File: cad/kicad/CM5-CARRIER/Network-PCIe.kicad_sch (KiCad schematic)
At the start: 59 parts, among them J610 74991114412, J611 74991114412, J612 74991114412, J613 74991114412, J620 AW7915-NP1_WIFI6_4T4R, J621 PCIE_SPARE_TEST, U601 PI7C9X2G608GP, U611 LAN7430, U612 LAN7430, U613 LAN7430, U630 TPD4E05U06DQA, U631 TPD4E05U06DQA, U632 TPD4E05U06DQA, U633 TPD4E05U06DQA, U634 TPD4E05U06DQA, U635 TPD4E05U06DQA, U636 TPD4E05U06DQA, U637 TPD4E05U06DQA, Y611 25MHz, Y612 25MHz, Y613 25MHz

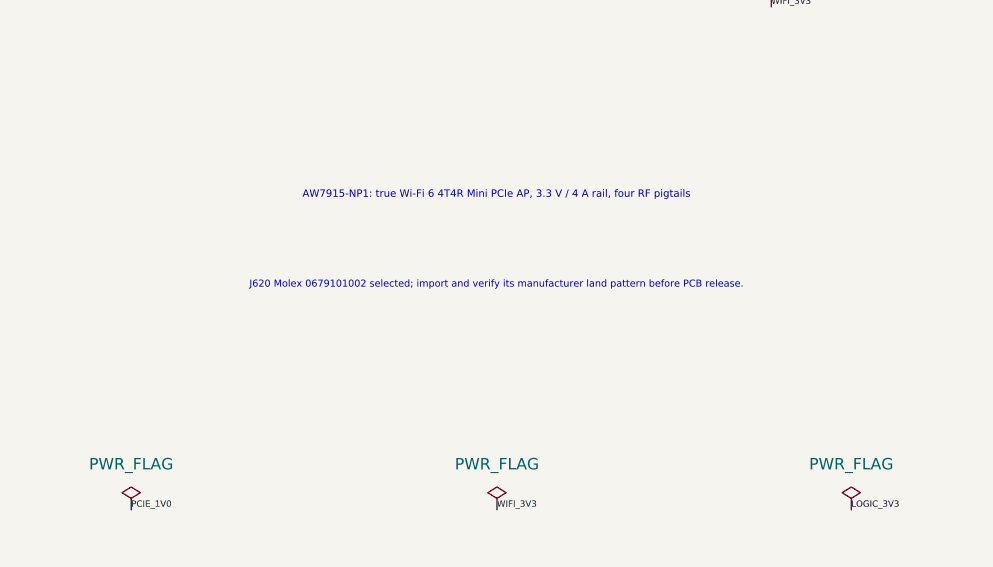
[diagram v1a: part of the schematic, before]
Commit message: Add controlled connector footprint audit
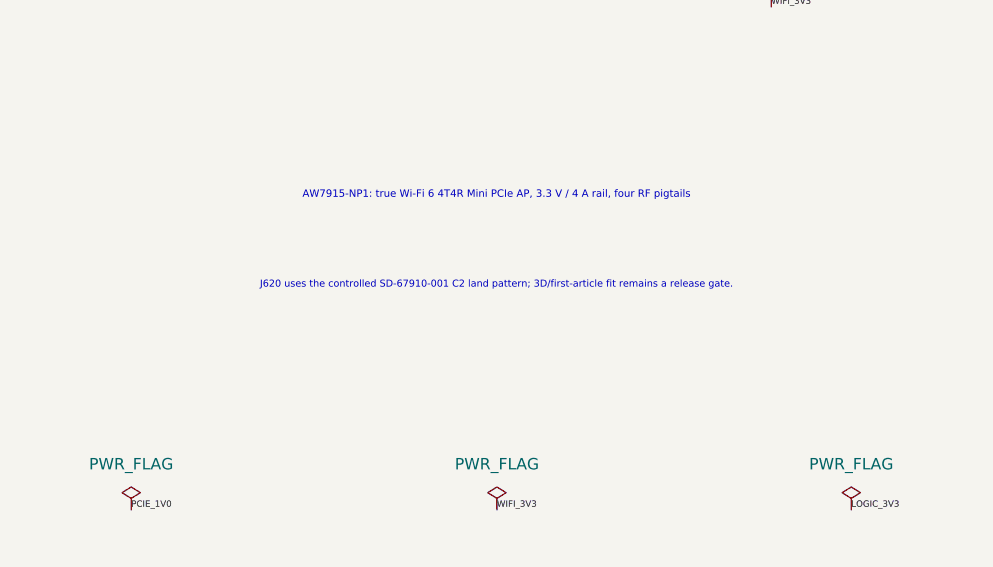
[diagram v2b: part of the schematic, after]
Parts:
- J620: footprint (none) -> CM5Carrier:Molex_0679101002_Mini_PCIe
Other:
- note added: "J620 uses the controlled SD-67910-001 C2 land pattern; 3D/first-article fit remains a release gate."
- note removed: "J620 Molex 0679101002 selected; import and verify its manufacturer land pattern before PCB release."
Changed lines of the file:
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@@
 			)
 		)
+		(property "Footprint" "CM5Carrier:Molex_0679101002_Mini_PCIe"
+			(at 515.62 420.37 0.0000)
+			(effects
+				(font
+					(size 1.27 1.27)
+				)
+				(hide yes)
+			)
+		)
 		(property "Manufacturer" "Molex"
 			(at 518.16 425.4499 0)
@@
 		)
 	)
-	(text "J620 Molex 0679101002 selected; import and verify its manufacturer land pattern before PCB release."
+	(text "J620 uses the controlled SD-67910-001 C2 land pattern; 3D/first-article fit remains a release gate."
 		(exclude_from_sim no)
 		(at 400 525 0.0000)

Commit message: Complete A1 detailed carrier and audio capture
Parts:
- removed C6121: 10uF, symbol Device:C
- removed C6122: 100nF, symbol Device:C
- removed J621: PCIE_SPARE_TEST, symbol Connector_Generic:Conn_02x06_Odd_Even
- removed L6121: 3.3uH, symbol Device:L
- removed U636: TPD4E05U06DQA, Package_SON:USON-10_2.5x1.0mm_P0.5mm, symbol Power_Protection:TPD4E05U06DQA
- removed Y611, Y613: 25MHz, symbol Device:Crystal
- added C6114, C6115, C6124, C6125, C6134, C6135: 15pF C0G, Capacitor_SMD:C_0402_1005Metric, symbol Device:C
- added J612: 74991114412, CM5Carrier:T_Wurth_WE-RJ45LAN_74991114412, symbol WurthRJ45:74991114412
- added R6122: 6.04k 1%, Resistor_SMD:R_0603_1608Metric, symbol Device:R
- added R657: 330R, Resistor_SMD:R_0603_1608Metric, symbol Device:R
- added Y611, Y612, Y613: 25MHz / 10pF / -40..85C, Crystal:Crystal_SMD_3225-4Pin_3.2x2.5mm, symbol CM5Carrier:Crystal_GND24_3225
- C601, C602, C603, C604, C6112, C6132: footprint (none) -> Capacitor_SMD:C_0402_1005Metric; MPN (none) -> C1005X7R1H104K050BB; Manufacturer (none) -> TDK
- C6111, C6131: value 10uF -> 10uF 25V X5R; footprint (none) -> Capacitor_SMD:C_0603_1608Metric; MPN (none) -> GRM188R61E106MA73D; Manufacturer (none) -> Murata
- C6113, C6133: value 1uF ESR>=0.1R -> 1uF 35V X5R / ESR <1R; footprint (none) -> Capacitor_SMD:C_0402_1005Metric; MPN (none) -> GRM155R6YA105KE11D; Manufacturer (none) -> Murata
- C6121: renamed from R6121; value 200R 1% -> 10uF 25V X5R; footprint (none) -> Capacitor_SMD:C_0603_1608Metric; symbol Device:R -> Device:C; MPN (none) -> GRM188R61E106MA73D; Manufacturer (none) -> Murata
- C6122: renamed from R6122; value 6.04k 1% -> 100nF; footprint (none) -> Capacitor_SMD:C_0402_1005Metric; symbol Device:R -> Device:C; MPN (none) -> C1005X7R1H104K050BB; Manufacturer (none) -> TDK
- C6123: renamed from Y612; value 25MHz -> 1uF 35V X5R / ESR <1R; footprint (none) -> Capacitor_SMD:C_0402_1005Metric; symbol Device:Crystal -> Device:C; MPN (none) -> GRM155R6YA105KE11D; Manufacturer (none) -> Murata
- L6111, L6131: value 3.3uH -> 3.3uH / 2.37A min; footprint (none) -> CM5Carrier:TDK_VLS3012HBX; MPN (none) -> VLS3012HBX-3R3M-N; Manufacturer (none) -> TDK
- L6121: renamed from C6123; value 1uF ESR>=0.1R -> 3.3uH / 2.37A min; footprint (none) -> CM5Carrier:TDK_VLS3012HBX; symbol Device:C -> Device:L; MPN (none) -> VLS3012HBX-3R3M-N; Manufacturer (none) -> TDK
- R601: footprint (none) -> Resistor_SMD:R_0603_1608Metric; MPN (none) -> RC0603FR-074K7L; Manufacturer (none) -> Yageo
- R602, R603: footprint (none) -> Resistor_SMD:R_0603_1608Metric; MPN (none) -> RC0603FR-071K43L; Manufacturer (none) -> Yageo
- R604: footprint (none) -> Resistor_SMD:R_0603_1608Metric; MPN (none) -> RC0603FR-07475RL; Manufacturer (none) -> Yageo
- R605, R606: footprint (none) -> Resistor_SMD:R_0603_1608Metric; MPN (none) -> RC0603FR-072K2L; Manufacturer (none) -> Yageo
- R607: footprint (none) -> Resistor_SMD:R_0603_1608Metric; MPN (none) -> RC0603JR-070RL; Manufacturer (none) -> Yageo
- R6111, R6131: footprint (none) -> Resistor_SMD:R_0603_1608Metric; MPN (none) -> RC0603FR-07200RL; Manufacturer (none) -> Yageo
- R6112, R6132: footprint (none) -> Resistor_SMD:R_0603_1608Metric; MPN (none) -> RC0603FR-076K04L; Manufacturer (none) -> Yageo
- R6121: renamed from J612; value 74991114412 -> 200R 1%; footprint CM5Carrier:T_Wurth_WE-RJ45LAN_74991114412 -> Resistor_SMD:R_0603_1608Metric; symbol WurthRJ45:74991114412 -> Device:R; MPN 74991114412 -> RC0603FR-07200RL; Manufacturer Wurth Elektronik -> Yageo
- R620: footprint (none) -> Resistor_SMD:R_0603_1608Metric; MPN (none) -> RC0603FR-0710KL; Manufacturer (none) -> Yageo
- R650, R651, R652, R653, R654, R655, R656: footprint (none) -> Resistor_SMD:R_0603_1608Metric; MPN (none) -> RC0603FR-07330RL; Manufacturer (none) -> Yageo
- U601: MPN (none) -> PI7C9X2G608GPCNJEX; Manufacturer (none) -> Diodes Incorporated
- U611, U612, U613: MPN LAN7430/Y9X -> LAN7430T-I/Y9X
- U630, U631, U632, U633, U634, U635, U637: MPN TPD4E05U06DQA -> TPD4E05U06DQAR
- U636: renamed from R657; value 330R -> TPD4E05U06DQA; footprint (none) -> Package_SON:USON-10_2.5x1.0mm_P0.5mm; symbol Device:R -> Power_Protection:TPD4E05U06DQA; MPN (none) -> TPD4E05U06DQAR; Manufacturer (none) -> Texas Instruments
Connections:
- net CHASSIS_GND: now also J612.S1 (SHIELD1), J612.S2 (SHIELD2); no longer R6121.S1 (SHIELD1), R6121.S2 (SHIELD2)
- net GND: now also C6123.2, R6121.2, U636.3 (GND), U636.8 (GND), C6114.2, C6115.2, C6124.2, C6125.2, C6134.2, C6135.2, J612.1 (GND), R6122.2, Y611.2 (GND), Y611.4 (GND), Y612.2 (GND), Y612.4 (GND), Y613.2 (GND), Y613.4 (GND); no longer L6121.2, R6121.1 (GND)
- net LAN1_1V2: now also C6121.1, C6122.1, L6121.2
- net LAN1_2V5: now also C6123.1; no longer L6121.1
- net LAN1_ISET: now also R6122.1; no longer C6122.1
- net LAN1_LED0: now also J612.12 (LED1_Y+/G-); no longer R6121.12 (LED1_Y+/G-)
- net LAN1_LED1: now also J612.14 (LED2_Y+/G-); no longer R6121.14 (LED2_Y+/G-)
- net LAN1_LED_A1: now also J612.11 (LED1_Y-/G+); no longer R6121.11 (LED1_Y-/G+)
- net LAN1_LED_A2: now also J612.13 (LED2_Y-/G+); no longer R6121.13 (LED2_Y-/G+)
- net LAN1_MDI_A_N: now also J612.3 (D1-); no longer R6121.3 (D1-)
- net LAN1_MDI_A_P: now also J612.2 (D1+); no longer R6121.2 (D1+)
- net LAN1_MDI_B_N: now also J612.5 (D2-); no longer R6121.5 (D2-)
- net LAN1_MDI_B_P: now also J612.4 (D2+); no longer R6121.4 (D2+)
- net LAN1_MDI_C_N: now also J612.7 (D3-); no longer R6121.7 (D3-)
- net LAN1_MDI_C_P: now also J612.6 (D3+); no longer R6121.6 (D3+)
- net LAN1_MDI_D_N: now also J612.9 (D4-); no longer R6121.9 (D4-)
- net LAN1_MDI_D_P: now also J612.8 (D4+); no longer R6121.8 (D4+)
- net LAN1_RESREF: now also R6121.1; no longer C6121.1
- net LAN1_SW_NODE: now also L6121.1
- net LAN1_XI: now also C6124.1, Y612.1 (XI); no longer C6123.1
- net LAN1_XO: now also C6125.1, Y612.3 (XO); no longer C6123.2
- net LAN2_LED_A2: now also R657.2; no longer U636.2
- net LAN2_MDI_A_N: now also U636.2 (D1-)
- net LAN2_MDI_A_P: now also U636.1 (D1+)
- net LAN2_MDI_B_N: now also U636.5 (D2-)
- net LAN2_MDI_B_P: now also U636.4 (D2+)
- net LAN2_XI: now also C6134.1, Y613.1 (XI)
- net LAN2_XO: now also C6135.1, Y613.3 (XO)
- net NET_3V3: now also R657.1; no longer U636.1
- net WAN2_XI: now also C6114.1, Y611.1 (XI)
- net WAN2_XO: now also C6115.1, Y611.3 (XO)
- net PCIE_SPARE_CLKREQ_N: no longer names the net of U601.A1 (CLKREQ_L[5])
- net PCIE_SPARE_PERST_N: no longer names the net of U601.M4 (DWNRST_L[5])
- net PCIE_SPARE_REFCLK_N: no longer names the net of U601.L14 (REFCLKON[7])
- net PCIE_SPARE_REFCLK_P: no longer names the net of U601.L13 (REFCLKOP[7])
- net PCIE_SPARE_RX_N: no longer names the net of U601.N6 (PETN[1])
- net PCIE_SPARE_RX_P: no longer names the net of U601.P6 (PETP[1])
- net PCIE_SPARE_TX_N: no longer names the net of U601.N5 (PERN[1])
- net PCIE_SPARE_TX_P: no longer names the net of U601.P5 (PERP[1])
- no-connect marks 111 -> 119
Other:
- note added: "3. WI-FI AP MINI PCIE 4T4R"
- note added: "Hold PERST# low until 3.3 V, 1.0 V, and 100 MHz REFCLK are stable for at least 100 ms."
- note added: "Switch port 5 is disabled and unrouted to avoid PCIe Gen2 stubs and an unsafe generic test header."
- note removed: "3. WI-FI AP MINI PCIE 4T4R + SPARE PORT"
- note removed: "Port 5 is a controlled factory/test option; do not fit a cable header in production by default."

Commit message: Audit schematic logic against controlled datasheets
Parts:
- removed C6111, C6121: 10uF 25V X5R, Capacitor_SMD:C_0603_1608Metric, symbol Device:C
- removed C6112: 100nF, Capacitor_SMD:C_0402_1005Metric, symbol Device:C
- removed J620: AW7915-NP1_WIFI6_4T4R, CM5Carrier:Molex_0679101002_Mini_PCIe, symbol Connector:Bus_PCI_Express_Mini
- removed L6111: 3.3uH / 2.37A min, CM5Carrier:TDK_VLS3012HBX, symbol Device:L
- removed R601: 4.7k, Resistor_SMD:R_0603_1608Metric, symbol Device:R
- removed R602, R603: 1.43k 1%, Resistor_SMD:R_0603_1608Metric, symbol Device:R
- removed U612: LAN7430, Package_DFN_QFN:QFN-48-1EP_7x7mm_P0.5mm_EP5.3x5.3mm_ThermalVias, symbol CM5Carrier:LAN7430
- added C602, C603, C604, C605, C606, C607, C608, C609, C610, C611, C61110, C61111, C61112, C61113, C61115, C61210, C61211, C61212, C61213, C61214, C61215, C61310, C61311, C61312, C61313, C61314, C61315, C6601, C6602, C6603, C6604, C6605, C6606, C6607, C6608, C6609, C6610, C6611, C6612, C6613, C6614, C6615, C6616, C6617, C6618, C6619, C6620, C6621, C6622, C6623, C6624, C6625, C6626: 100nF, Capacitor_SMD:C_0402_1005Metric, symbol Device:C
- added C6114, C6115: 15pF C0G, Capacitor_SMD:C_0402_1005Metric, symbol Device:C
- added C6116, C6117, C6118, C6119, C6126, C6127, C6128, C6129, C6136, C6137, C6138, C6139: 10nF, Capacitor_SMD:C_0603_1608Metric, symbol Device:C
- added C6131, C6630, C6631: 22uF 10V X7R, Capacitor_SMD:C_0805_2012Metric, symbol Device:C
- added FB6111, FB6121, FB6122, FB6131, FB6132: 220R ferrite, Inductor_SMD:L_0805_2012Metric, symbol Device:FerriteBead
- added J611: 74991114412, CM5Carrier:T_Wurth_WE-RJ45LAN_74991114412, symbol WurthRJ45:74991114412
- added J620: AW7915-NP1_WIFI6_4T4R, CM5Carrier:Molex_0679101002_Mini_PCIe, symbol CM5Carrier:Mini_PCIe_52
- added R608: 100k, Resistor_SMD:R_0603_1608Metric, symbol Device:R
- added R6113, R6123, R6133: 10k, Resistor_SMD:R_0603_1608Metric, symbol Device:R
- added R6121: 200R 1%, Resistor_SMD:R_0603_1608Metric, symbol Device:R
- added R6122: 6.04k 1%, Resistor_SMD:R_0603_1608Metric, symbol Device:R
- added U606: SN74LVC1G11DBVR, Package_TO_SOT_SMD:SOT-23-6, symbol 74xGxx:74LVC1G11
- added U613: LAN7430, Package_DFN_QFN:QFN-48-1EP_7x7mm_P0.5mm_EP5.3x5.3mm_ThermalVias, symbol CM5Carrier:LAN7430
- added U635, U637: TPD4E05U06DQA, Package_SON:USON-10_2.5x1.0mm_P0.5mm, symbol Power_Protection:TPD4E05U06DQA
- added Y612: 25MHz / 10pF / -40..85C, Crystal:Crystal_SMD_3225-4Pin_3.2x2.5mm, symbol CM5Carrier:Crystal_GND24_3225
- C6111: renamed from R6122; value 6.04k 1% -> 22uF 10V X7R; footprint Resistor_SMD:R_0603_1608Metric -> Capacitor_SMD:C_0805_2012Metric; symbol Device:R -> Device:C; MPN RC0603FR-076K04L -> GRM21BR71A226ME44L; Manufacturer Yageo -> Murata
- C61114: renamed from U613; value LAN7430 -> 100nF; footprint Package_DFN_QFN:QFN-48-1EP_7x7mm_P0.5mm_EP5.3x5.3mm_ThermalVias -> Capacitor_SMD:C_0402_1005Metric; symbol CM5Carrier:LAN7430 -> Device:C; MPN LAN7430T-I/Y9X -> C1005X7R1H104K050BB; Manufacturer Microchip -> TDK
- C6112: renamed from Y612; value 25MHz / 10pF / -40..85C -> 100nF; footprint Crystal:Crystal_SMD_3225-4Pin_3.2x2.5mm -> Capacitor_SMD:C_0402_1005Metric; symbol CM5Carrier:Crystal_GND24_3225 -> Device:C; MPN ABM8-25.000MHZ-10-D1G-T -> C1005X7R1H104K050BB; Manufacturer Abracon -> TDK
- C6121: renamed from U637; value TPD4E05U06DQA -> 22uF 10V X7R; footprint Package_SON:USON-10_2.5x1.0mm_P0.5mm -> Capacitor_SMD:C_0805_2012Metric; symbol Power_Protection:TPD4E05U06DQA -> Device:C; MPN TPD4E05U06DQAR -> GRM21BR71A226ME44L; Manufacturer Texas Instruments -> Murata
- C6627: renamed from C6114; value 15pF C0G -> 100nF; MPN GRM1555C1H150JA01D -> C1005X7R1H104K050BB; Manufacturer Murata -> TDK
- C6628: renamed from C6115; value 15pF C0G -> 100nF; MPN GRM1555C1H150JA01D -> C1005X7R1H104K050BB; Manufacturer Murata -> TDK
- C6629: renamed from J611; value 74991114412 -> 100nF; footprint CM5Carrier:T_Wurth_WE-RJ45LAN_74991114412 -> Capacitor_SMD:C_0402_1005Metric; symbol WurthRJ45:74991114412 -> Device:C; MPN 74991114412 -> C1005X7R1H104K050BB; Manufacturer Wurth Elektronik -> TDK
- FB6112: renamed from U635; value TPD4E05U06DQA -> 220R ferrite; footprint Package_SON:USON-10_2.5x1.0mm_P0.5mm -> Inductor_SMD:L_0805_2012Metric; symbol Power_Protection:TPD4E05U06DQA -> Device:FerriteBead; MPN TPD4E05U06DQAR -> BLM21PG221SN1D; Manufacturer Texas Instruments -> Murata
- L6111: renamed from R6121; value 200R 1% -> 3.3uH / 2.37A min; footprint Resistor_SMD:R_0603_1608Metric -> CM5Carrier:TDK_VLS3012HBX; symbol Device:R -> Device:L; MPN RC0603FR-07200RL -> VLS3012HBX-3R3M-N; Manufacturer Yageo -> TDK
- R601: renamed from R604; value 475R 1% -> 4.7k; MPN RC0603FR-07475RL -> RC0603FR-074K7L
- R602: renamed from R605; value 2.2k -> 1.43k 1%; MPN RC0603FR-072K2L -> RC0603FR-071K43L
- R603: renamed from R606; value 2.2k -> 1.43k 1%; MPN RC0603FR-072K2L -> RC0603FR-071K43L
- R604: renamed from R607; value 0R -> 475R 1%; MPN RC0603JR-070RL -> RC0603FR-07475RL
- R605: renamed from C601; value 100nF -> 2.2k; footprint Capacitor_SMD:C_0402_1005Metric -> Resistor_SMD:R_0603_1608Metric; symbol Device:C -> Device:R; MPN C1005X7R1H104K050BB -> RC0603FR-072K2L; Manufacturer TDK -> Yageo
- R606: renamed from C602; value 100nF -> 2.2k; footprint Capacitor_SMD:C_0402_1005Metric -> Resistor_SMD:R_0603_1608Metric; symbol Device:C -> Device:R; MPN C1005X7R1H104K050BB -> RC0603FR-072K2L; Manufacturer TDK -> Yageo
- R607: renamed from C603; value 100nF -> 0R; footprint Capacitor_SMD:C_0402_1005Metric -> Resistor_SMD:R_0603_1608Metric; symbol Device:C -> Device:R; MPN C1005X7R1H104K050BB -> RC0603JR-070RL; Manufacturer TDK -> Yageo
- U612: renamed from C6131; value 10uF 25V X5R -> LAN7430; footprint Capacitor_SMD:C_0603_1608Metric -> Package_DFN_QFN:QFN-48-1EP_7x7mm_P0.5mm_EP5.3x5.3mm_ThermalVias; symbol Device:C -> CM5Carrier:LAN7430; MPN GRM188R61E106MA73D -> LAN7430T-I/Y9X; Manufacturer Murata -> Microchip
- renumbered C604 to C601
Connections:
- net WAN2_LED3 is gone; now on net GND: U611.35 (VAUX_DET/GPIO3/LED3/TCK)
- net CHASSIS_GND: now also J611.S1 (SHIELD1), J611.S2 (SHIELD2); no longer C6629.S1 (SHIELD1), C6629.S2 (SHIELD2)
- net GND: now also C6121.2, C6629.2, R602.2, R603.2, R607.2, U612.15 (GD_1), U612.18 (GD_2), U612.22 (GD_3), U612.30 (TEST), U612.35 (VAUX_DET/GPIO3/LED3/TCK), U612.49 (VSS_EP), C611.2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; no longer C61114.15 (GD_1), C61114.18 (GD_2), C61114.22 (GD_3), C61114.30 (TEST), C61114.49 (VSS_EP), C6112.4 (GND), C6121.3 (GND), C6121.8 (GND), C6629.1 (GND), FB6112.3 (GND), FB6112.8 (GND), L6111.2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
- net LAN1_1V2: now also C6121.1, U612.13 (VDD12CORE), U612.31 (VDD12CORE), U612.34 (VDD12_SW_FB), U612.40 (VDD12CORE), FB6121.1
- net LAN1_ISET: now also U612.48 (ISET), R6122.1; no longer C6111.1
- net LAN1_LED0: now also U612.38 (EECS/GPIO0/LED0/TDI)
- net LAN1_LED1: now also U612.37 (EEDIO/GPIO1/LED1/TDO)
- net LAN1_MDI_A_N: now also U612.3 (TXRXM_A)
- net LAN1_MDI_A_P: now also U612.2 (TXRXP_A)
- net LAN1_MDI_B_N: now also U612.6 (TXRXM_B)
- net LAN1_MDI_B_P: now also U612.5 (TXRXP_B)
- net LAN1_MDI_C_N: now also U612.8 (TXRXM_C), U635.2 (D1-); no longer FB6112.2 (D1-)
- net LAN1_MDI_C_P: now also U612.7 (TXRXP_C), U635.1 (D1+); no longer FB6112.1 (D1+)
- net LAN1_MDI_D_N: now also U612.11 (TXRXM_D), U635.5 (D2-); no longer FB6112.5 (D2-)
- net LAN1_MDI_D_P: now also U612.10 (TXRXP_D), U635.4 (D2+); no longer FB6112.4 (D2+)
- net LAN1_PCIE_CLKREQ_N: now also U612.42 (CLKREQ#)
- net LAN1_PCIE_PERST_N: now also U612.44 (PERST#)
- net LAN1_PCIE_REFCLK_N: now also U612.26 (PCIE_CLK_M)
- net LAN1_PCIE_REFCLK_P: now also U612.25 (PCIE_CLK_P)
- net LAN1_PCIE_RX_N: now also U612.17 (PCIE_RX_M), C61213.2; no longer U601.B9 (PETN[5])
- net LAN1_PCIE_RX_P: now also U612.16 (PCIE_RX_P), C61212.2; no longer U601.A9 (PETP[5])
- net LAN1_PCIE_TX_N: now also C61215.2
- net LAN1_PCIE_TX_P: now also C61214.2
- net LAN1_RESET_LOCAL_N: now also U612.29 (RESET_N), R6123.2
- net LAN1_RESREF: now also U612.24 (RESREF), R6121.1; no longer L6111.1
- net LAN1_SW_NODE: now also U612.32 (VDD12_SW_OUT)
- net LAN1_XI: now also U612.47 (XI), Y612.1 (XI); no longer C6112.1 (XI)
- net LAN1_XO: now also U612.46 (XO), Y612.3 (XO); no longer C6112.3 (XO)
- net LAN2_1V2: now also C6131.1, FB6131.1, U613.13 (VDD12CORE), U613.31 (VDD12CORE), U613.34 (VDD12_SW_FB), U613.40 (VDD12CORE); no longer C61114.13 (VDD12CORE), C61114.14 (VP), C61114.20 (VPTX), C61114.31 (VDD12CORE), C61114.34 (VDD12_SW_FB), C61114.4 (AVDDL_1), C61114.40 (VDD12CORE), C61114.45 (AVDD12), C61114.9 (AVDDL_2), U612.1
- net LAN2_ISET: now also U613.48 (ISET); no longer C61114.48 (ISET)
- net LAN2_LED0: now also U613.38 (EECS/GPIO0/LED0/TDI); no longer C61114.38 (EECS/GPIO0/LED0/TDI)
- net LAN2_LED1: now also U613.37 (EEDIO/GPIO1/LED1/TDO); no longer C61114.37 (EEDIO/GPIO1/LED1/TDO)
- net LAN2_MDI_A_N: now also U613.3 (TXRXM_A); no longer C61114.3 (TXRXM_A)
- net LAN2_MDI_A_P: now also U613.2 (TXRXP_A); no longer C61114.2 (TXRXP_A)
- net LAN2_MDI_B_N: now also U613.6 (TXRXM_B); no longer C61114.6 (TXRXM_B)
- net LAN2_MDI_B_P: now also U613.5 (TXRXP_B); no longer C61114.5 (TXRXP_B)
- net LAN2_MDI_C_N: now also U613.8 (TXRXM_C), U637.2 (D1-); no longer C61114.8 (TXRXM_C), C6121.2 (D1-)
- net LAN2_MDI_C_P: now also U613.7 (TXRXP_C), U637.1 (D1+); no longer C61114.7 (TXRXP_C), C6121.1 (D1+)
- net LAN2_MDI_D_N: now also U613.11 (TXRXM_D), U637.5 (D2-); no longer C61114.11 (TXRXM_D), C6121.5 (D2-)
- net LAN2_MDI_D_P: now also U613.10 (TXRXP_D), U637.4 (D2+); no longer C61114.10 (TXRXP_D), C6121.4 (D2+)
- net LAN2_PCIE_CLKREQ_N: now also U613.42 (CLKREQ#); no longer C61114.42 (CLKREQ#)
- net LAN2_PCIE_PERST_N: now also U613.44 (PERST#); no longer C61114.44 (PERST#)
- net LAN2_PCIE_REFCLK_N: now also U613.26 (PCIE_CLK_M); no longer C61114.26 (PCIE_CLK_M)
- net LAN2_PCIE_REFCLK_P: now also U613.25 (PCIE_CLK_P); no longer C61114.25 (PCIE_CLK_P)
- net LAN2_PCIE_RX_N: now also C61313.2, U613.17 (PCIE_RX_M); no longer C61114.17 (PCIE_RX_M), U601.B6 (PETN[6])
- net LAN2_PCIE_RX_P: now also C61312.2, U613.16 (PCIE_RX_P); no longer C61114.16 (PCIE_RX_P), U601.A6 (PETP[6])
- net LAN2_PCIE_TX_N: now also C61315.2; no longer C61114.21 (PCIE_TX_M)
- net LAN2_PCIE_TX_P: now also C61314.2; no longer C61114.19 (PCIE_TX_P)
- net LAN2_RESET_LOCAL_N: now also R6133.2, U613.29 (RESET_N); no longer C61114.29 (RESET_N)
- net LAN2_RESREF: now also U613.24 (RESREF); no longer C61114.24 (RESREF)
- net LAN2_SW_NODE: now also U613.32 (VDD12_SW_OUT); no longer C61114.32 (VDD12_SW_OUT)
- net LAN2_XI: now also U613.47 (XI); no longer C61114.47 (XI)
- net LAN2_XO: now also U613.46 (XO); no longer C61114.46 (XO)
- net LOGIC_3V3: now also R605.2, R606.2, C611.1, U606.5 (VCC); no longer R602.2, R603.2
- net NET_3V3: now also C6628.1, C6629.1, R601.2, U612.28 (VDD_REG_IN), U612.33 (VDD_SW_IN), U612.39 (VDDVARIO), U612.41 (VDD_OTP), C6116.1, C6117.1, C6118.1, C6119.1, C6126.1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; no longer C61114.28 (VDD_REG_IN), C61114.33 (VDD_SW_IN), C61114.39 (VDDVARIO), C61114.41 (VDD_OTP)
- net PCIE_1V0: now also C6627.1, C6603.1, C6604.1, C6605.1, C6606.1, C6607.1, C6608.1, C6610.1, C6611.1, C6613.1, C6614.1, C6616.1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
- net PCIE_MODE_606_HIGH: now also R601.1
- net PCIE_UP_CLKREQ_N: now also R607.1; no longer R604.1
- net PCIE_UP_PERST_N: now also R608.1, U606.4
- net PCIE_UP_RX_N_CM5: now also C608.2; no longer U601.N4 (PETN[0])
- net PCIE_UP_RX_P_CM5: now also C607.2; no longer U601.P4 (PETP[0])
- net PCIE_UP_TX_N_CM5: now also C606.1; no longer U601.N3 (PERN[0])
- net PCIE_UP_TX_P_CM5: now also C605.1; no longer U601.P3 (PERP[0])
- net PCIE_UP_WAKE_N: now also U612.43 (WAKE#), J620.1 (WAKE#), U613.43 (WAKE#); no longer C61114.43 (WAKE#)
- net SW_IREF: now also R604.1; no longer R601.1
- net SW_REFCLK0_IN_N: now also C602.2; no longer R606.2
- net SW_REFCLK0_IN_P: now also C601.2; no longer R605.2
- net SW_REFCLK1_IN_N: now also C604.2; no longer C601.2
- net SW_REFCLK1_IN_P: now also C603.2; no longer R607.2
- net SW_REFCLK1_RAW_N: now also C602.1; no longer R606.1
- net SW_REFCLK1_RAW_P: now also C601.1; no longer R605.1
- net SW_REFCLK2_RAW_N: now also C604.1; no longer C601.1
- net SW_REFCLK2_RAW_P: now also C603.1; no longer R607.1
- net SW_REXT0: now also R603.1
- net SW_REXT1: now also R602.1
- net SYS_I2C7_SCL: now also R606.1, J620.30 (SMB_CLK); no longer R603.1
- net SYS_I2C7_SDA: now also R605.1, J620.32 (SMB_DATA); no longer R602.1
- net LAN1_2V5 renamed LAN1_2V5_OUT
- removed net LAN2_2V5: C61114.1 (AVDDH_1), C61114.12 (AVDDH_2), C61114.23 (VPH), C61114.27 (VDD25_REG_OUT), C6133.1
- removed net LAN2_LED2: C61114.36 (EECLK/GPIO2/LED2/TMS/ADV_PM_DISABLE)
- removed net LAN2_LED3: C61114.35 (VAUX_DET/GPIO3/LED3/TCK)
- net WAN2_2V5 renamed WAN2_2V5_A
- new net LAN1_1V2_A: C61210.1, FB6121.2, U612.14 (VP), U612.20 (VPTX), U612.4 (AVDDL_1), U612.45 (AVDD12), U612.9 (AVDDL_2)
- new net LAN1_2V5_A: C61211.1, FB6122.2, U612.1 (AVDDH_1), U612.12 (AVDDH_2), U612.23 (VPH)
- new net LAN1_EP_TX_N: C61215.1, U612.21 (PCIE_TX_M)
- new net LAN1_EP_TX_P: C61214.1, U612.19 (PCIE_TX_P)
- new net LAN1_SW_TX_N: C61213.1, U601.B9 (PETN[5])
- new net LAN1_SW_TX_P: C61212.1, U601.A9 (PETP[5])
- new net LAN2_1V2_A: C61310.1, FB6131.2, U613.14 (VP), U613.20 (VPTX), U613.4 (AVDDL_1), U613.45 (AVDD12), U613.9 (AVDDL_2)
- new net LAN2_2V5_A: C61311.1, FB6132.2, U613.1 (AVDDH_1), U613.12 (AVDDH_2), U613.23 (VPH)
- new net LAN2_2V5_OUT: C6133.1, FB6132.1, U613.27 (VDD25_REG_OUT)
- new net LAN2_EP_TX_N: C61315.1, U613.21 (PCIE_TX_M)
- new net LAN2_EP_TX_P: C61314.1, U613.19 (PCIE_TX_P)
- new net LAN2_SW_TX_N: C61313.1, U601.B6 (PETN[6])
- new net LAN2_SW_TX_P: C61312.1, U601.A6 (PETP[6])
- new net NET_3V3_PG: U606.3
- new net PCIE_1V0_PG: U606.6
- new net PCIE_UP_PERST_CMD_N: U606.1
- new net PCIE_UP_SW_RX_N: C606.2, U601.N3 (PERN[0])
- new net PCIE_UP_SW_RX_P: C605.2, U601.P3 (PERP[0])
- new net PCIE_UP_SW_TX_N: C608.1, U601.N4 (PETN[0])
- new net PCIE_UP_SW_TX_P: C607.1, U601.P4 (PETP[0])
- new net WAN2_1V2_A: C61110.1, FB6111.2, U611.14 (VP), U611.20 (VPTX), U611.4 (AVDDL_1), U611.45 (AVDD12), U611.9 (AVDDL_2)
- new net WAN2_2V5_OUT: C6113.1, FB6112.1, U611.27 (VDD25_REG_OUT)
- new net WAN2_EP_TX_N: C61115.1, U611.21 (PCIE_TX_M)
- new net WAN2_EP_TX_P: C61114.1, U611.19 (PCIE_TX_P)
- new net WAN2_SW_TX_N: C61113.1, U601.B11 (PETN[4])
- new net WAN2_SW_TX_P: C61112.1, U601.A11 (PETP[4])
- new net WIFI_SW_TX_N: C610.1, U601.B4 (PETN[7])
- new net WIFI_SW_TX_P: C609.1, U601.A4 (PETP[7])
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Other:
- note added: "AW7915-NP1: Wi-Fi 6 4T4R Mini PCIe AP; vendor maximum 9.1 W and 3.5 A recommended; dedicated rail is 3.3 V / 4 A."
- note added: "CM5 firmware/root-complex timing must keep the request low until REFCLK and rails have been stable for at least 100 ms."
- note added: "HARDWARE-QUALIFIED UPSTREAM RESET"
- note added: "LAN1: RESET_N pulled high; PCIe TX pairs AC-coupled; analog 1.2 V/2.5 V rails ferrite-isolated."
- note added: "LAN1: pin 35 tied low disables D3cold PME; pin 36 floats on its internal pull-down so advanced PCIe PM remains enabled."
- note added: "LAN2: RESET_N pulled high; PCIe TX pairs AC-coupled; analog 1.2 V/2.5 V rails ferrite-isolated."
- note added: "LAN2: pin 35 tied low disables D3cold PME; pin 36 floats on its internal pull-down so advanced PCIe PM remains enabled."
- note added: "U601 rail bypass: one 100 nF per supply ball plus 22 uF bulk on 1.0 V and 3.3 V."
- note added: "U601C: every 1.0 V / 3.3 V / ground ball shown; one 100 nF capacitor is assigned to every supply ball"
- note added: "U606 asserts switch PERST# unless the CM5 request and both PCIe rail power-good signals are high."
- note added: "WAN2: RESET_N pulled high; PCIe TX pairs AC-coupled; analog 1.2 V/2.5 V rails ferrite-isolated."
- note added: "WAN2: pin 35 tied low disables D3cold PME; pin 36 floats on its internal pull-down so advanced PCIe PM remains enabled."
- note removed: "AW7915-NP1: true Wi-Fi 6 4T4R Mini PCIe AP, 3.3 V / 4 A rail, four RF pigtails"
- note removed: "Hold PERST# low until 3.3 V, 1.0 V, and 100 MHz REFCLK are stable for at least 100 ms."
- note removed: "U601C: every 1.0 V / 3.3 V / ground ball shown; place decoupling per ball group"
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
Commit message: Implement direct socketed dual-SIM daughterboard
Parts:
- removed C61212: 100nF, Capacitor_SMD:C_0402_1005Metric, symbol Device:C
- removed C6123: 1uF 35V X5R / ESR <1R, Capacitor_SMD:C_0402_1005Metric, symbol Device:C
- removed C6134, C6135: 15pF C0G, Capacitor_SMD:C_0402_1005Metric, symbol Device:C
- removed C6136, C6137, C6138, C6139: 10nF, Capacitor_SMD:C_0603_1608Metric, symbol Device:C
- removed FB6131: 220R ferrite, Inductor_SMD:L_0805_2012Metric, symbol Device:FerriteBead
- removed J611, J613: 74991114412, CM5Carrier:T_Wurth_WE-RJ45LAN_74991114412, symbol WurthRJ45:74991114412
- removed R6121: 200R 1%, Resistor_SMD:R_0603_1608Metric, symbol Device:R
- removed R6122: 6.04k 1%, Resistor_SMD:R_0603_1608Metric, symbol Device:R
- removed R650: 330R, Resistor_SMD:R_0603_1608Metric, symbol Device:R
- removed U633: TPD4E05U06DQA, Package_SON:USON-10_2.5x1.0mm_P0.5mm, symbol Power_Protection:TPD4E05U06DQA
- removed Y612: 25MHz / 10pF / -40..85C, Crystal:Crystal_SMD_3225-4Pin_3.2x2.5mm, symbol CM5Carrier:Crystal_GND24_3225
- added C6124, C6125: 15pF C0G, Capacitor_SMD:C_0402_1005Metric, symbol Device:C
- added C6126, C6127: 10nF, Capacitor_SMD:C_0603_1608Metric, symbol Device:C
- added C61310, C61311, C61312, C61313, C61314: 100nF, Capacitor_SMD:C_0402_1005Metric, symbol Device:C
- added J611, J612, J613: V8BR-1AX1-GH, CM5Carrier:Bel_V8BR_1AX1_GH, symbol CM5Carrier:Bel_V8BR_1AX1_GH
- added R6133: 10k, Resistor_SMD:R_0603_1608Metric, symbol Device:R
- added R653: 330R, Resistor_SMD:R_0603_1608Metric, symbol Device:R
- added U611: LAN7430, Package_DFN_QFN:QFN-48-1EP_7x7mm_P0.5mm_EP5.3x5.3mm_ThermalVias, symbol CM5Carrier:LAN7430
- added U636: TPD4E05U06DQA, Package_SON:USON-10_2.5x1.0mm_P0.5mm, symbol Power_Protection:TPD4E05U06DQA
- C61212: renamed from J612; value 74991114412 -> 100nF; footprint CM5Carrier:T_Wurth_WE-RJ45LAN_74991114412 -> Capacitor_SMD:C_0402_1005Metric; symbol WurthRJ45:74991114412 -> Device:C; MPN 74991114412 -> C1005X7R1H104K050BB; Manufacturer Wurth Elektronik -> TDK
- C6123: renamed from C6124; value 15pF C0G -> 1uF 35V X5R / ESR <1R; MPN GRM1555C1H150JA01D -> GRM155R6YA105KE11D
- C61315: renamed from U636; value TPD4E05U06DQA -> 100nF; footprint Package_SON:USON-10_2.5x1.0mm_P0.5mm -> Capacitor_SMD:C_0402_1005Metric; symbol Power_Protection:TPD4E05U06DQA -> Device:C; MPN TPD4E05U06DQAR -> C1005X7R1H104K050BB; Manufacturer Texas Instruments -> TDK
- C6134: renamed from FB6132; value 220R ferrite -> 15pF C0G; footprint Inductor_SMD:L_0805_2012Metric -> Capacitor_SMD:C_0402_1005Metric; symbol Device:FerriteBead -> Device:C; MPN BLM21PG221SN1D -> GRM1555C1H150JA01D
- C6135: renamed from C61310; value 100nF -> 15pF C0G; MPN C1005X7R1H104K050BB -> GRM1555C1H150JA01D; Manufacturer TDK -> Murata
- C6136: renamed from C61311; value 100nF -> 10nF; footprint Capacitor_SMD:C_0402_1005Metric -> Capacitor_SMD:C_0603_1608Metric; MPN C1005X7R1H104K050BB -> GRM188R71H103KA01D; Manufacturer TDK -> Murata
- C6137: renamed from R6133; value 10k -> 10nF; footprint Resistor_SMD:R_0603_1608Metric -> Capacitor_SMD:C_0603_1608Metric; symbol Device:R -> Device:C; MPN RC0603FR-0710KL -> GRM188R71H103KA01D; Manufacturer Yageo -> Murata
- C6138: renamed from C61312; value 100nF -> 10nF; footprint Capacitor_SMD:C_0402_1005Metric -> Capacitor_SMD:C_0603_1608Metric; MPN C1005X7R1H104K050BB -> GRM188R71H103KA01D; Manufacturer TDK -> Murata
- C6139: renamed from C61313; value 100nF -> 10nF; footprint Capacitor_SMD:C_0402_1005Metric -> Capacitor_SMD:C_0603_1608Metric; MPN C1005X7R1H104K050BB -> GRM188R71H103KA01D; Manufacturer TDK -> Murata
- FB6131: renamed from C61314; value 100nF -> 220R ferrite; footprint Capacitor_SMD:C_0402_1005Metric -> Inductor_SMD:L_0805_2012Metric; symbol Device:C -> Device:FerriteBead; MPN C1005X7R1H104K050BB -> BLM21PG221SN1D; Manufacturer TDK -> Murata
- FB6132: renamed from C61315; value 100nF -> 220R ferrite; footprint Capacitor_SMD:C_0402_1005Metric -> Inductor_SMD:L_0805_2012Metric; symbol Device:C -> Device:FerriteBead; MPN C1005X7R1H104K050BB -> BLM21PG221SN1D; Manufacturer TDK -> Murata
- J610: value 74991114412 -> V8BR-1AX1-GH; footprint CM5Carrier:T_Wurth_WE-RJ45LAN_74991114412 -> CM5Carrier:Bel_V8BR_1AX1_GH; symbol WurthRJ45:74991114412 -> CM5Carrier:Bel_V8BR_1AX1_GH; MPN 74991114412 -> V8BR-1AX1-GH; Manufacturer Wurth Elektronik -> Bel
- R6121: renamed from C6125; value 15pF C0G -> 200R 1%; footprint Capacitor_SMD:C_0402_1005Metric -> Resistor_SMD:R_0603_1608Metric; symbol Device:C -> Device:R; MPN GRM1555C1H150JA01D -> RC0603FR-07200RL; Manufacturer Murata -> Yageo
- R6122: renamed from C6126; value 10nF -> 6.04k 1%; footprint Capacitor_SMD:C_0603_1608Metric -> Resistor_SMD:R_0603_1608Metric; symbol Device:C -> Device:R; MPN GRM188R71H103KA01D -> RC0603FR-076K04L; Manufacturer Murata -> Yageo
- R650: renamed from U611; value LAN7430 -> 330R; footprint Package_DFN_QFN:QFN-48-1EP_7x7mm_P0.5mm_EP5.3x5.3mm_ThermalVias -> Resistor_SMD:R_0603_1608Metric; symbol CM5Carrier:LAN7430 -> Device:R; MPN LAN7430T-I/Y9X -> RC0603FR-07330RL; Manufacturer Microchip -> Yageo
- U633: renamed from R653; value 330R -> TPD4E05U06DQA; footprint Resistor_SMD:R_0603_1608Metric -> Package_SON:USON-10_2.5x1.0mm_P0.5mm; symbol Device:R -> Power_Protection:TPD4E05U06DQA; MPN RC0603FR-07330RL -> TPD4E05U06DQAR; Manufacturer Yageo -> Texas Instruments
- Y612: renamed from C6127; value 10nF -> 25MHz / 10pF / -40..85C; footprint Capacitor_SMD:C_0603_1608Metric -> Crystal:Crystal_SMD_3225-4Pin_3.2x2.5mm; symbol Device:C -> CM5Carrier:Crystal_GND24_3225; MPN GRM188R71H103KA01D -> ABM8-25.000MHZ-10-D1G-T; Manufacturer Murata -> Abracon
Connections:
- net CHASSIS_GND: now also J610.21 (SHIELD), J610.22 (SHIELD), J611.21 (SHIELD), J611.22 (SHIELD), J612.21 (SHIELD), J612.22 (SHIELD), J613.21 (SHIELD), J613.22 (SHIELD); no longer C61212.S1 (SHIELD1), C61212.S2 (SHIELD2), J610.S1 (SHIELD1), J610.S2 (SHIELD2)
- net GND: now also C6134.2, C6137.2, C6138.2, C6139.2, J610.12 (TRCT1), J610.6 (TRCT2), J610.7 (TRCT4), U633.3 (GND), U633.8 (GND), Y612.4 (GND), C6124.2, C6125.2, C6126.2, C6127.2, C61310.2, C61311.2, J611.1 (TRCT3), J611.12 (TRCT1), J611.6 (TRCT2), J611.7 (TRCT4), J612.1 (TRCT3), J612.12 (TRCT1), J612.6 (TRCT2), J612.7 (TRCT4), J613.1 (TRCT3), J613.12 (TRCT1), J613.6 (TRCT2), J613.7 (TRCT4), U611.15 (GD_1), U611.18 (GD_2), U611.22 (GD_3), U611.30 (TEST), U611.35 (VAUX_DET/GPIO3/LED3/TCK), U611.49 (VSS_EP), U636.3 (GND), U636.8 (GND); no longer C61212.1 (GND), C61315.3 (GND), C61315.8 (GND), R650.15 (GD_1), R650.18 (GD_2), R650.22 (GD_3), R650.30 (TEST), R650.35 (VAUX_DET/GPIO3/LED3/TCK), R650.49 (VSS_EP)
- net LAN1_2V5_OUT: now also C6123.1
- net LAN1_ISET: now also R6122.1
- net LAN1_LED0: now also J612.17 (LED1-); no longer C61212.12 (LED1_Y+/G-)
- net LAN1_LED1: now also J612.19 (LED2-); no longer C61212.14 (LED2_Y+/G-)
- net LAN1_LED_A1: now also J612.18 (LED1+); no longer C61212.11 (LED1_Y-/G+)
- net LAN1_LED_A2: now also J612.20 (LED2+); no longer C61212.13 (LED2_Y-/G+)
- net LAN1_MDI_A_N: now also J612.10 (TRD1-); no longer C61212.3 (D1-)
- net LAN1_MDI_A_P: now also J612.11 (TRD1+); no longer C61212.2 (D1+)
- net LAN1_MDI_B_N: now also J612.5 (TRD2-); no longer C61212.5 (D2-)
- net LAN1_MDI_B_P: now also J612.4 (TRD2+); no longer C61212.4 (D2+)
- net LAN1_MDI_C_N: now also J612.2 (TRD3-); no longer C61212.7 (D3-)
- net LAN1_MDI_C_P: now also J612.3 (TRD3+); no longer C61212.6 (D3+)
- net LAN1_MDI_D_N: now also J612.9 (TRD4-); no longer C61212.9 (D4-)
- net LAN1_MDI_D_P: now also J612.8 (TRD4+); no longer C61212.8 (D4+)
- net LAN1_PCIE_RX_P: now also C61212.2
- net LAN1_RESREF: now also R6121.1
- net LAN1_SW_TX_P: now also C61212.1
- net LAN1_XI: now also Y612.1 (XI), C6124.1; no longer C6123.1
- net LAN1_XO: now also Y612.3 (XO), C6125.1; no longer R6121.1
- net LAN2_1V2: now also FB6131.1
- net LAN2_1V2_A: now also FB6131.2, C61310.1; no longer C6135.1
- net LAN2_2V5_A: now also FB6132.2, C61311.1; no longer C6134.2, C6136.1
- net LAN2_2V5_OUT: now also FB6132.1; no longer C6134.1
- net LAN2_EP_TX_N: now also C61315.1; no longer FB6132.1
- net LAN2_EP_TX_P: now also C61314.1; no longer FB6131.1
- net LAN2_LED0: now also J613.17 (LED1-)
- net LAN2_LED1: now also J613.19 (LED2-)
- net LAN2_LED_A1: now also J613.18 (LED1+)
- net LAN2_LED_A2: now also J613.20 (LED2+)
- net LAN2_MDI_A_N: now also J613.10 (TRD1-), U636.2 (D1-); no longer C61315.2 (D1-)
- net LAN2_MDI_A_P: now also J613.11 (TRD1+), U636.1 (D1+); no longer C61315.1 (D1+)
- net LAN2_MDI_B_N: now also J613.5 (TRD2-), U636.5 (D2-); no longer C61315.5 (D2-)
- net LAN2_MDI_B_P: now also J613.4 (TRD2+), U636.4 (D2+); no longer C61315.4 (D2+)
- net LAN2_MDI_C_N: now also J613.2 (TRD3-)
- net LAN2_MDI_C_P: now also J613.3 (TRD3+)
- net LAN2_MDI_D_N: now also J613.9 (TRD4-)
- net LAN2_MDI_D_P: now also J613.8 (TRD4+)
- net LAN2_PCIE_RX_N: now also C61313.2; no longer C6139.2
- net LAN2_PCIE_RX_P: now also C61312.2; no longer C6138.2
- net LAN2_PCIE_TX_N: now also C61315.2; no longer FB6132.2
- net LAN2_PCIE_TX_P: now also C61314.2; no longer FB6131.2
- net LAN2_RESET_LOCAL_N: now also R6133.2; no longer C6137.2
- net LAN2_SW_TX_N: now also C61313.1; no longer C6139.1
- net LAN2_SW_TX_P: now also C61312.1; no longer C6138.1
- net LAN2_XI: now also C6134.1
- net LAN2_XO: now also C6135.1
- net NET_3V3: now also C6136.1, C6138.1, C6139.1, R650.1, C6126.1, C6127.1, R6133.1, R653.1, U611.28 (VDD_REG_IN), U611.33 (VDD_SW_IN), U611.39 (VDDVARIO), U611.41 (VDD_OTP); no longer R6122.1, R650.28 (VDD_REG_IN), R650.33 (VDD_SW_IN), R650.39 (VDDVARIO), R650.41 (VDD_OTP), U633.1, Y612.1
- net PCIE_UP_WAKE_N: now also U611.43 (WAKE#); no longer R650.43 (WAKE#)
- net WAN1_LED0: now also J610.17 (LED1-); no longer J610.12 (LED1_Y+/G-)
- net WAN1_LED1: now also J610.19 (LED2-); no longer J610.14 (LED2_Y+/G-)
- net WAN1_LED_A1: now also J610.18 (LED1+), R650.2; no longer J610.11 (LED1_Y-/G+)
- net WAN1_LED_A2: now also J610.20 (LED2+); no longer J610.13 (LED2_Y-/G+)
- net WAN1_MDI0_N: now also J610.10 (TRD1-); no longer J610.3 (D1-)
- net WAN1_MDI0_P: now also J610.11 (TRD1+); no longer J610.2 (D1+)
- net WAN1_MDI2_N: now also J610.2 (TRD3-); no longer J610.7 (D3-)
- net WAN1_MDI2_P: now also J610.3 (TRD3+); no longer J610.6 (D3+)
- net WAN2_1V2: now also U611.13 (VDD12CORE), U611.31 (VDD12CORE), U611.34 (VDD12_SW_FB), U611.40 (VDD12CORE); no longer R650.13 (VDD12CORE), R650.31 (VDD12CORE), R650.34 (VDD12_SW_FB), R650.40 (VDD12CORE)
- net WAN2_1V2_A: now also U611.14 (VP), U611.20 (VPTX), U611.4 (AVDDL_1), U611.45 (AVDD12), U611.9 (AVDDL_2); no longer R650.14 (VP), R650.20 (VPTX), R650.4 (AVDDL_1), R650.45 (AVDD12), R650.9 (AVDDL_2)
- net WAN2_2V5_A: now also U611.1 (AVDDH_1), U611.12 (AVDDH_2), U611.23 (VPH); no longer R650.1 (AVDDH_1), R650.12 (AVDDH_2), R650.23 (VPH)
- net WAN2_2V5_OUT: now also U611.27 (VDD25_REG_OUT); no longer R650.27 (VDD25_REG_OUT)
- net WAN2_EP_TX_N: now also U611.21 (PCIE_TX_M); no longer R650.21 (PCIE_TX_M)
- net WAN2_EP_TX_P: now also U611.19 (PCIE_TX_P); no longer R650.19 (PCIE_TX_P)
- net WAN2_ISET: now also U611.48 (ISET); no longer R650.48 (ISET)
- net WAN2_LED0: now also J611.17 (LED1-), U611.38 (EECS/GPIO0/LED0/TDI); no longer R650.38 (EECS/GPIO0/LED0/TDI)
- net WAN2_LED1: now also J611.19 (LED2-), U611.37 (EEDIO/GPIO1/LED1/TDO); no longer R650.37 (EEDIO/GPIO1/LED1/TDO)
- net WAN2_LED_A1: now also J611.18 (LED1+)
- net WAN2_LED_A2: now also J611.20 (LED2+), R653.2; no longer U633.2
- net WAN2_MDI_A_N: now also J611.10 (TRD1-), U611.3 (TXRXM_A); no longer R650.3 (TXRXM_A)
- net WAN2_MDI_A_P: now also J611.11 (TRD1+), U611.2 (TXRXP_A); no longer R650.2 (TXRXP_A)
- net WAN2_MDI_B_N: now also J611.5 (TRD2-), U611.6 (TXRXM_B); no longer R650.6 (TXRXM_B)
- net WAN2_MDI_B_P: now also J611.4 (TRD2+), U611.5 (TXRXP_B); no longer R650.5 (TXRXP_B)
- net WAN2_MDI_C_N: now also U633.2 (D1-), J611.2 (TRD3-), U611.8 (TXRXM_C); no longer R650.8 (TXRXM_C)
- net WAN2_MDI_C_P: now also U633.1 (D1+), J611.3 (TRD3+), U611.7 (TXRXP_C); no longer R650.7 (TXRXP_C)
- net WAN2_MDI_D_N: now also U633.5 (D2-), J611.9 (TRD4-), U611.11 (TXRXM_D); no longer R650.11 (TXRXM_D)
- net WAN2_MDI_D_P: now also U633.4 (D2+), J611.8 (TRD4+), U611.10 (TXRXP_D); no longer R650.10 (TXRXP_D)
- net WAN2_PCIE_CLKREQ_N: now also U611.42 (CLKREQ#); no longer R650.42 (CLKREQ#)
- net WAN2_PCIE_PERST_N: now also U611.44 (PERST#); no longer R650.44 (PERST#)
- net WAN2_PCIE_REFCLK_N: now also U611.26 (PCIE_CLK_M); no longer R650.26 (PCIE_CLK_M)
- net WAN2_PCIE_REFCLK_P: now also U611.25 (PCIE_CLK_P); no longer R650.25 (PCIE_CLK_P)
- net WAN2_PCIE_RX_N: now also U611.17 (PCIE_RX_M); no longer R650.17 (PCIE_RX_M)
- net WAN2_PCIE_RX_P: now also U611.16 (PCIE_RX_P); no longer R650.16 (PCIE_RX_P)
- net WAN2_RESET_LOCAL_N: now also U611.29 (RESET_N); no longer R650.29 (RESET_N)
- net WAN2_RESREF: now also U611.24 (RESREF); no longer R650.24 (RESREF)
- net WAN2_SW_NODE: now also U611.32 (VDD12_SW_OUT); no longer R650.32 (VDD12_SW_OUT)
- net WAN2_XI: now also U611.47 (XI); no longer R650.47 (XI)
- net WAN2_XO: now also U611.46 (XO); no longer R650.46 (XO)
- no-connect marks 121 -> 137
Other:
- note added: "LAN1: vertical V8BR-1AX1-GH; PHY CTs to GND, PoE CTs NC, shield to chassis"
- note added: "LAN2: vertical V8BR-1AX1-GH; PHY CTs to GND, PoE CTs NC, shield to chassis"
- note added: "WAN1: vertical V8BR-1AX1-GH; PHY CTs to GND, PoE CTs NC, shield to chassis"
- note added: "WAN2: vertical V8BR-1AX1-GH; PHY CTs to GND, PoE CTs NC, shield to chassis"
- note removed: "LAN1: 74991114412 voltage-mode 1 GbE; shields direct to chassis, PHY-side residual ESD"
- note removed: "LAN2: 74991114412 voltage-mode 1 GbE; shields direct to chassis, PHY-side residual ESD"
- note removed: "WAN1: 74991114412 voltage-mode 1 GbE; shields direct to chassis, PHY-side residual ESD"
- note removed: "WAN2: 74991114412 voltage-mode 1 GbE; shields direct to chassis, PHY-side residual ESD"
- moved on the sheet: C6123, C6135, C6136, C6138, C6139
